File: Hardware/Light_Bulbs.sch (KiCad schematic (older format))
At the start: 29 parts, among them U1 PIC18F23K22

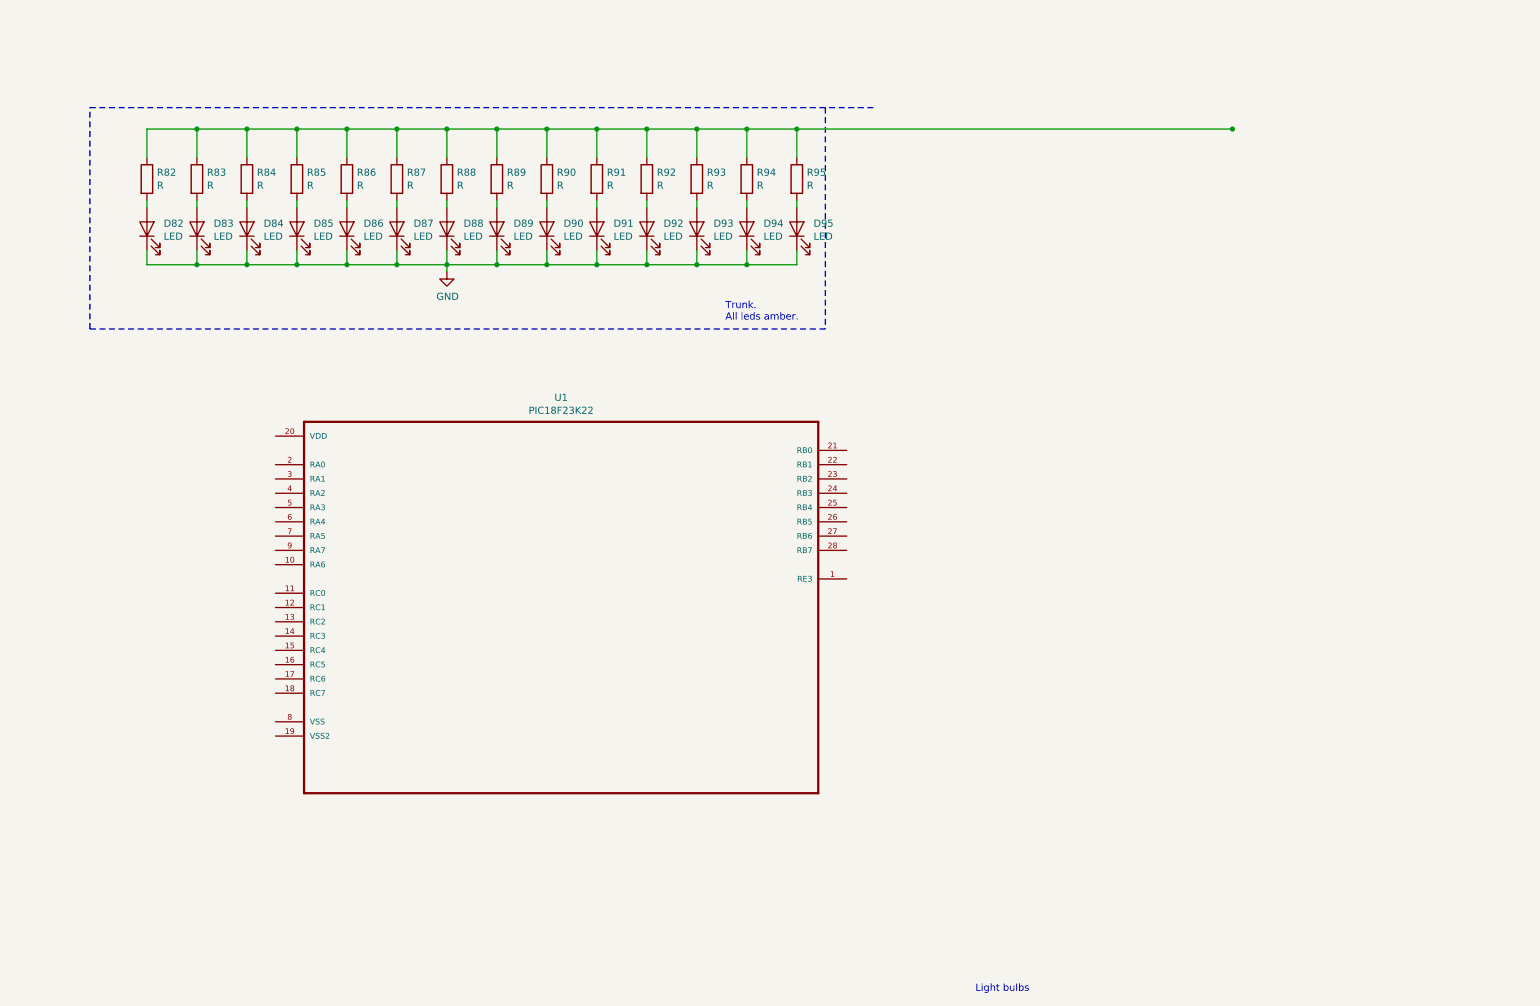
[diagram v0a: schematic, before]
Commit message: Added light bulbs schematic.
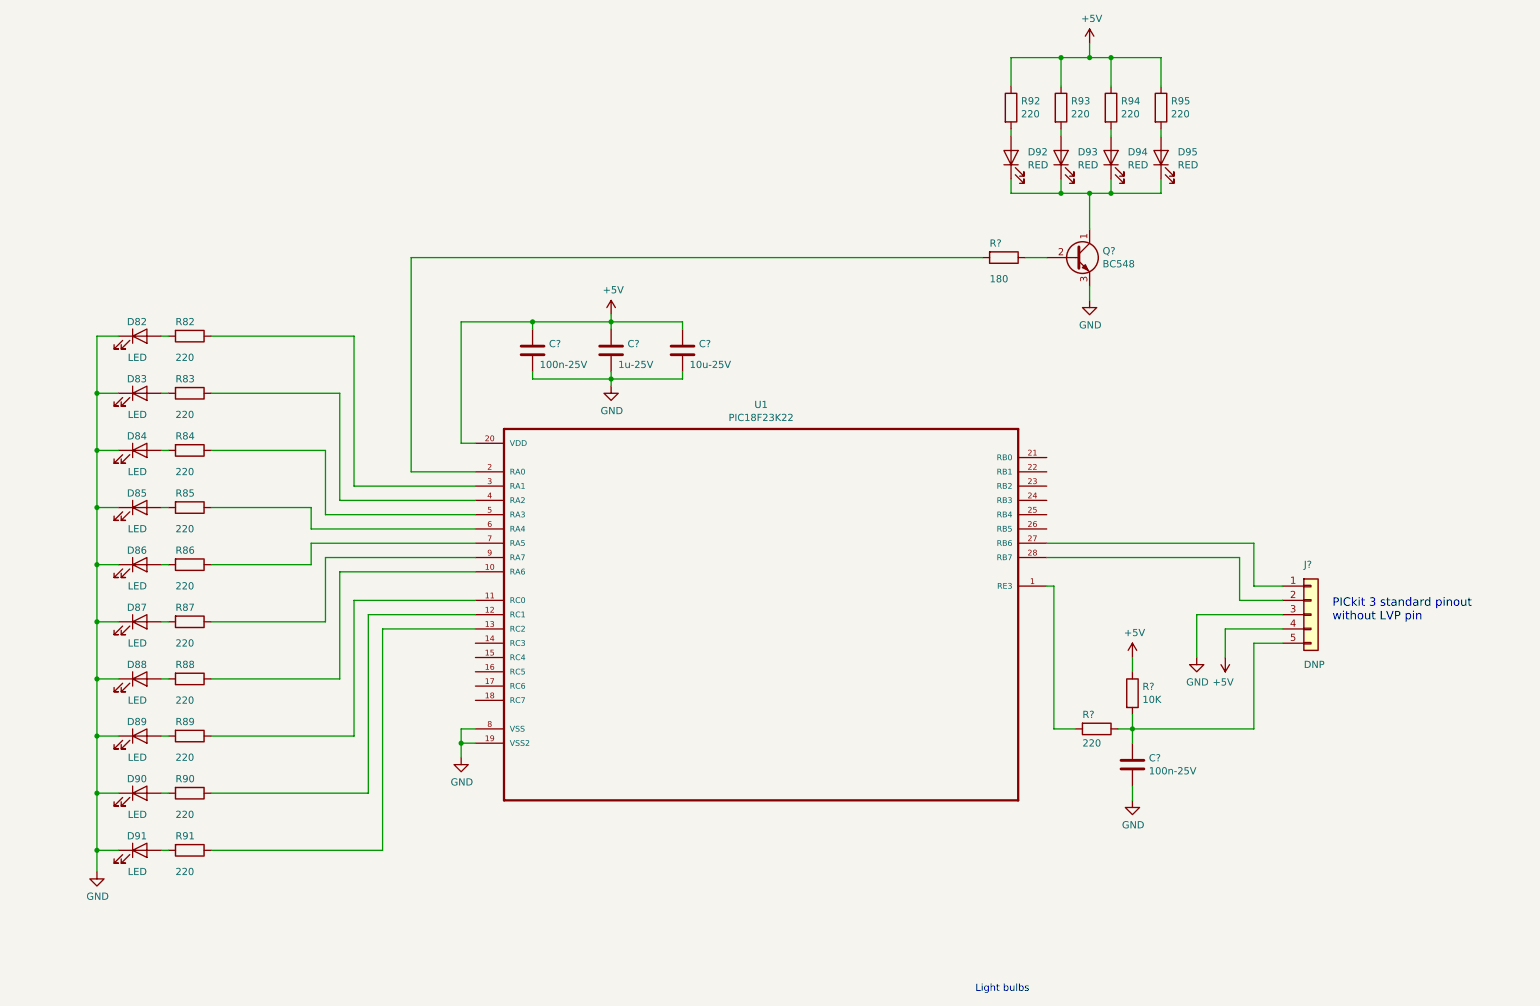
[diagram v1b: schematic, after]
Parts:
- added C?: 1u-25V, Capacitor_THT:C_Disc_D5.0mm_W2.5mm_P5.00mm, symbol Device:C
- added C?: 10u-25V, Capacitor_THT:C_Disc_D5.0mm_W2.5mm_P5.00mm, symbol Device:C
- added C? (x2): 100n-25V, Capacitor_THT:C_Disc_D5.0mm_W2.5mm_P5.00mm, symbol Device:C
- added J?: DNP, Connector_PinHeader_2.54mm:PinHeader_1x05_P2.54mm_Vertical, symbol Connector_Generic:Conn_01x05
- added Q?: BC548, Package_TO_SOT_THT:TO-92_Inline, symbol Transistor_BJT:BC548
- added R?: 180, Resistor_THT:R_Axial_DIN0207_L6.3mm_D2.5mm_P7.62mm_Horizontal, symbol Device:R
- added R?: 10K, Resistor_THT:R_Axial_DIN0207_L6.3mm_D2.5mm_P7.62mm_Horizontal, symbol Device:R
- added R?: 220, Resistor_THT:R_Axial_DIN0207_L6.3mm_D2.5mm_P7.62mm_Horizontal, symbol Device:R
- D92, D93, D94, D95: value LED -> RED
- R82, R83, R84, R85, R86, R87, R88, R89, R90, R91, R92, R93, R94, R95: value R -> 220
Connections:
- net GND: now also U1.19 (VSS2), U1.8 (VSS), C?.2, C?.2, C?.2, C?.2, J?.3 (Pin_3), Q?.3 (E); no longer D92.1 (K), D93.1 (K), D94.1 (K), D95.1 (K)
- net at U1.1 (RE3): now also R?.2
- net at U1.10 (RA6): now also R88.1
- net at U1.11 (RC0): now also R89.1
- net at U1.12 (RC1): now also R90.1
- net at U1.13 (RC2): now also R91.1
- net at U1.2 (RA0): now also R?.2
- net +5V: now reaches U1.20 (VDD)
- net +5V: now also R92.1, R93.1, R94.1, R95.1, C?.1, C?.1, C?.1, J?.4 (Pin_4), R?.1
- net at U1.27 (RB6): now also J?.1 (Pin_1)
- net at U1.28 (RB7): now also J?.2 (Pin_2)
- net at U1.3 (RA1): now also R82.1
- net at U1.4 (RA2): now also R83.1
- net at U1.5 (RA3): now also R84.1
- net at U1.6 (RA4): now also R85.1
- net at U1.7 (RA5): now also R86.1
- net at U1.9 (RA7): now also R87.1
- new net: C?.1, J?.5 (Pin_5), R?.1, R?.2
- new net: D92.1 (K), D93.1 (K), D94.1 (K), D95.1 (K), Q?.1 (C)
- new net: Q?.2 (B), R?.1
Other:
- note added: "PICkit 3 standard pinout\nwithout LVP pin"
- note removed: "Trunk.\nAll leds amber."
- moved on the sheet: D82, D83, D84, D85, D86, D87, D88, D89, D90, D91, D92, D93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

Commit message: Reorganized light bulbs connections to ease routing and placed microcontroller and related parts.
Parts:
- gave numbers to parts that had none: 9
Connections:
- net labels added: Bulb_0, Bulb_1, Bulb_2, Bulb_3, Bulb_4, Bulb_5, Bulb_6, Bulb_7, Bulb_8, Bulb_9, Star
- wire segments 127 -> 116
- no-connect marks 0 -> 11
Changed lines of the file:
@@
 Connection ~ 8350 1900
 $Comp
-L Transistor_BJT:BC548 Q?
+L Transistor_BJT:BC548 Q1
 U 1 1 5DE42A41
 P 8100 2350
-F 0 "Q?" H 8291 2396 50  0000 L CNN
+F 0 "Q1" H 8291 2396 50  0000 L CNN
 F 1 "BC548" H 8291 2305 50  0000 L CNN
 F 2 "Package_TO_SOT_THT:TO-92_Inline" H 8300 2275 50  0001 L CIN
@@
 P 8500 5400
 AR Path="/5DE1DFF6/5DFA145B" Ref="R?"  Part="1"
-AR Path="/5DE2A82E/5DFA145B" Ref="R?"  Part="1"
-F 0 "R?" H 8570 5446 50  0000 L CNN
+AR Path="/5DE2A82E/5DFA145B" Ref="R98"  Part="1"
+F 0 "R98" H 8570 5446 50  0000 L CNN
 F 1 "10K" H 8570 5355 50  0000 L CNN
 F 2 "Resistor_THT:R_Axial_DIN0207_L6.3mm_D2.5mm_P7.62mm_Horizontal" V 8430 5400 50  0001 C CNN
@@
 P 8250 5650
 AR Path="/5DE1DFF6/5DFA8AD3" Ref="R?"  Part="1"
-AR Path="/5DE2A82E/5DFA8AD3" Ref="R?"  Part="1"
-F 0 "R?" V 8150 5550 50  0000 L CNN
+AR Path="/5DE2A82E/5DFA8AD3" Ref="R97"  Part="1"
+F 0 "R97" V 8150 5550 50  0000 L CNN
 F 1 "220" V 8350 5550 50  0000 L CNN
 F 2 "Resistor_THT:R_Axial_DIN0207_L6.3mm_D2.5mm_P7.62mm_Horizontal" V 8180 5650 50  0001 C CNN
@@
 $EndComp
 $Comp
-L Device:C C?
+L Device:C C4
 U 1 1 5DFB7332
 P 8500 5900
-F 0 "C?" H 8615 5946 50  0000 L CNN
+F 0 "C4" H 8615 5946 50  0000 L CNN
 F 1 "100n-25V" H 8615 5855 50  0000 L CNN
 F 2 "Capacitor_THT:C_Disc_D5.0mm_W2.5mm_P5.00mm" H 8538 5750 50  0001 C CNN
@@
 	9550 4650 9350 4650
 $Comp
-L Connector_Generic:Conn_01x05 J?
+L Connector_Generic:Conn_01x05 J1
 U 1 1 5DDF0B46
 P 9750 4850
-F 0 "J?" H 9700 5200 50  0000 L CNN
+F 0 "J1" H 9700 5200 50  0000 L CNN
 F 1 "DNP" H 9700 4500 50  0000 L CNN
 F 2 "Connector_PinHeader_2.54mm:PinHeader_1x05_P2.54mm_Vertical" H 9750 4850 50  0001 C CNN
@@
 $EndComp
 $Comp
-L power:GND #PWR?
+L power:GND #PWR0106
 U 1 1 5DDF5E99
 P 3800 5850
-F 0 "#PWR?" H 3800 5600 50  0001 C CNN
+F 0 "#PWR0106" H 3800 5600 50  0001 C CNN
 F 1 "GND" H 3805 5677 50  0000 C CNN
 F 2 "" H 3800 5850 50  0001 C CNN
@@
 	3800 3650 3900 3650
 $Comp
-L Device:C C?
+L Device:C C1
 U 1 1 5DE05CC3
 P 4300 3000
-F 0 "C?" H 4415 3046 50  0000 L CNN
+F 0 "C1" H 4415 3046 50  0000 L CNN
 F 1 "100n-25V" H 4350 2900 50  0000 L CNN
 F 2 "Capacitor_THT:C_Disc_D5.0mm_W2.5mm_P5.00mm" H 4338 2850 50  0001 C CNN
@@
 $EndComp
 $Comp
-L Device:C C?
+L Device:C C2
 U 1 1 5DDF165E
 P 4850 3000
-F 0 "C?" H 4965 3046 50  0000 L CNN
+F 0 "C2" H 4965 3046 50  0000 L CNN
 F 1 "1u-25V" H 4900 2900 50  0000 L CNN
 F 2 "Capacitor_THT:C_Disc_D5.0mm_W2.5mm_P5.00mm" H 4888 2850 50  0001 C CNN
@@
 $EndComp
 $Comp
-L Device:C C?
+L Device:C C3
 U 1 1 5DDF2D76
 P 5350 3000
-F 0 "C?" H 5465 3046 50  0000 L CNN
+F 0 "C3" H 5465 3046 50  0000 L CNN
 F 1 "10u-25V" H 5400 2900 50  0000 L CNN
 F 2 "Capacitor_THT:C_Disc_D5.0mm_W2.5mm_P5.00mm" H 5388 2850 50  0001 C CNN
@@
 $EndComp
 $Comp
-L power:GND #PWR?
+L power:GND #PWR0109
 U 1 1 5DF0D1D6
 P 4850 3250
-F 0 "#PWR?" H 4850 3000 50  0001 C CNN
+F 0 "#PWR0109" H 4850 3000 50  0001 C CNN
 F 1 "GND" H 4855 3077 50  0000 C CNN
 F 2 "" H 4850 3250 50  0001 C CNN
@@
 	5350 3200 5350 3150
 $Comp
-L power:+5V #PWR?
+L power:+5V #PWR0114
 U 1 1 5DF13942
 P 4850 2750
-F 0 "#PWR?" H 4850 2600 50  0001 C CNN
+F 0 "#PWR0114" H 4850 2600 50  0001 C CNN
 F 1 "+5V" H 4865 2923 50  0000 C CNN
 F 2 "" H 4850 2750 50  0001 C CNN
@@
 	3800 2800 3800 3650
 Connection ~ 4300 2800
-Wire Wire Line
-	3900 3950 3050 3950
-Wire Wire Line
-	3050 3950 3050 2900
-Wire Wire Line
-	3050 2900 2050 2900
-Wire Wire Line
-	2950 4050 2950 3300
-Wire Wire Line
-	2950 3300 2050 3300
-Wire Wire Line
-	2950 4050 3900 4050
-Wire Wire Line
-	2850 4150 2850 3700
-Wire Wire Line
-	2850 3700 2050 3700
-Wire Wire Line
-	2850 4150 3900 4150
-Wire Wire Line
-	2750 4250 2750 4100
-Wire Wire Line
-	2750 4100 2050 4100
-Wire Wire Line
-	2750 4250 3900 4250
-Wire Wire Line
-	2050 4500 2750 4500
-Wire Wire Line
-	2750 4500 2750 4350
-Wire Wire Line
-	2750 4350 3900 4350
-Wire Wire Line
-	3900 4450 2850 4450
-Wire Wire Line
-	2850 4450 2850 4900
-Wire Wire Line
-	2850 4900 2050 4900
-Wire Wire Line
-	2050 5300 2950 5300
-Wire Wire Line
-	2950 5300 2950 4550
-Wire Wire Line
-	2950 4550 3900 4550
-Wire Wire Line
-	2050 5700 3050 5700
-Wire Wire Line
-	3050 5700 3050 4750
-Wire Wire Line
-	3050 4750 3900 4750
-Wire Wire Line
-	3900 4850 3150 4850
-Wire Wire Line
-	3150 4850 3150 6100
-Wire Wire Line
-	3150 6100 2050 6100
-Wire Wire Line
-	2050 6500 3250 6500
-Wire Wire Line
-	3250 6500 3250 4950
-Wire Wire Line
-	3250 4950 3900 4950
 $Comp
 L Device:R R?
@@
 P 7600 2350
 AR Path="/5DE1DFF6/5DE4BB6C" Ref="R?"  Part="1"
-AR Path="/5DE2A82E/5DE4BB6C" Ref="R?"  Part="1"
-F 0 "R?" V 7500 2250 50  0000 L CNN
+AR Path="/5DE2A82E/5DE4BB6C" Ref="R96"  Part="1"
+F 0 "R96" V 7500 2250 50  0000 L CNN
 F 1 "180" V 7750 2250 50  0000 L CNN
 F 2 "Resistor_THT:R_Axial_DIN0207_L6.3mm_D2.5mm_P7.62mm_Horizontal" V 7530 2350 50  0001 C CNN
@@
 Wire Wire Line
 	7750 2350 7900 2350
-Wire Wire Line
-	7450 2350 3450 2350
-Wire Wire Line
-	3450 2350 3450 3850
-Wire Wire Line
-	3450 3850 3900 3850
-$Comp
-L power:GND #PWR?
+$Comp
+L power:GND #PWR0115
 U 1 1 5DE5620F
 P 1250 6650
-F 0 "#PWR?" H 1250 6400 50  0001 C CNN
+F 0 "#PWR0115" H 1250 6400 50  0001 C CNN
 F 1 "GND" H 1255 6477 50  0000 C CNN
 F 2 "" H 1250 6650 50  0001 C CNN
@@
 	1250 2900 1400 2900
 Connection ~ 1250 3300
+Text Label 3600 5050 0    50   ~ 0
+Star
+Wire Wire Line
+	7450 2350 7200 2350
+Text Label 7200 2350 0    50   ~ 0
+Star
+Wire Wire Line
+	3900 4950 3600 4950
+Wire Wire Line
+	3600 5050 3900 5050
+Text Label 3600 4950 0    50   ~ 0
+Bulb_0
+Wire Wire Line
+	2050 2900 2300 2900
+Text Label 2050 2900 0    50   ~ 0
+Bulb_0
+Wire Wire Line
+	2050 3300 2300 3300
+Wire Wire Line
+	2050 3700 2300 3700
+Wire Wire Line
+	2050 4100 2300 4100
+Wire Wire Line
+	2050 4500 2300 4500
+Wire Wire Line
+	2050 4900 2300 4900
+Wire Wire Line
+	2050 5300 2300 5300
+Wire Wire Line
+	2050 5700 2300 5700
+Wire Wire Line
+	2050 6100 2300 6100
+Wire Wire Line
+	2050 6500 2300 6500
+Text Label 2050 3700 0    50   ~ 0
+Bulb_1
+Wire Wire Line
+	3900 4850 3600 4850
+Text Label 3600 4850 0    50   ~ 0
+Bulb_1
+Text Label 2050 4500 0    50   ~ 0
+Bulb_2
+Wire Wire Line
+	3900 4750 3600 4750
+Text Label 3600 4750 0    50   ~ 0
+Bulb_2
+Text Label 2050 5300 0    50   ~ 0
+Bulb_3
+Wire Wire Line
+	3900 4550 3600 4550
+Text Label 3600 4550 0    50   ~ 0
+Bulb_3
+Text Label 2050 6100 0    50   ~ 0
+Bulb_4
+Wire Wire Line
+	3900 4450 3600 4450
+Text Label 3600 4450 0    50   ~ 0
+Bulb_4
+Text Label 2050 3300 0    50   ~ 0
+Bulb_9
+Wire Wire Line
+	3900 5150 3600 5150
+Text Label 3600 5150 0    50   ~ 0
+Bulb_9
+Text Label 2050 4100 0    50   ~ 0
+Bulb_8
+Wire Wire Line
+	3900 5250 3600 5250
+Text Label 3600 5250 0    50   ~ 0
+Bulb_8
+Text Label 2050 4900 0    50   ~ 0
+Bulb_7
+Wire Wire Line
+	3900 5350 3600 5350
+Text Label 3600 5350 0    50   ~ 0
+Bulb_7
+Text Label 2050 5700 0    50   ~ 0
+Bulb_6
+Text Label 7950 4150 0    50   ~ 0
+Bulb_6
+Wire Wire Line
+	7900 4150 8200 4150
+Text Label 2050 6500 0    50   ~ 0
+Bulb_5
+Wire Wire Line
+	7900 4250 8200 4250
+Text Label 7950 4250 0    50   ~ 0
+Bulb_5
+NoConn ~ 7900 3750
+NoConn ~ 7900 3850
+NoConn ~ 7900 3950
+NoConn ~ 7900 4050
+NoConn ~ 3900 3850
+NoConn ~ 3900 3950
+NoConn ~ 3900 4050
+NoConn ~ 3900 4150
+NoConn ~ 3900 4250
+NoConn ~ 3900 4350
+NoConn ~ 3900 5450
 $EndSCHEMATC

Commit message: Added micro USB B connector for power supply.
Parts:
- added J2: USB_B_Micro, Connector_USB:USB_Micro-B_Molex-105017-0001, symbol Connector:USB_B_Micro
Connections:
- wire segments 116 -> 123
- no-connect marks 11 -> 14
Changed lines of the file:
@@
 NoConn ~ 3900 4350
 NoConn ~ 3900 5450
+$Comp
+L Connector:USB_B_Micro J2
+U 1 1 60874A52
+P 3000 1450
+F 0 "J2" H 3057 1917 50  0000 C CNN
+F 1 "USB_B_Micro" H 3057 1826 50  0000 C CNN
+F 2 "Connector_USB:USB_Micro-B_Molex-105017-0001" H 3150 1400 50  0001 C CNN
+F 3 "~" H 3150 1400 50  0001 C CNN
+	1    3000 1450
+	1    0    0    -1
+$EndComp
+$Comp
+L power:+5V #PWR0118
+U 1 1 60877195
+P 3450 1200
+F 0 "#PWR0118" H 3450 1050 50  0001 C CNN
+F 1 "+5V" H 3465 1373 50  0000 C CNN
+F 2 "" H 3450 1200 50  0001 C CNN
+F 3 "" H 3450 1200 50  0001 C CNN
+	1    3450 1200
+	1    0    0    -1
+$EndComp
+Wire Wire Line
+	3300 1250 3450 1250
+Wire Wire Line
+	3450 1250 3450 1200
+Wire Wire Line
+	2900 1850 2900 1950
+Wire Wire Line
+	2900 1950 2950 1950
+Wire Wire Line
+	3000 1950 3000 1850
+$Comp
+L power:GND #PWR0119
+U 1 1 6088078F
+P 2950 2000
+F 0 "#PWR0119" H 2950 1750 50  0001 C CNN
+F 1 "GND" H 2955 1827 50  0000 C CNN
+F 2 "" H 2950 2000 50  0001 C CNN
+F 3 "" H 2950 2000 50  0001 C CNN
+	1    2950 2000
+	1    0    0    -1
+$EndComp
+Wire Wire Line
+	2950 2000 2950 1950
+Connection ~ 2950 1950
+Wire Wire Line
+	2950 1950 3000 1950
+NoConn ~ 3300 1450
+NoConn ~ 3300 1550
+NoConn ~ 3300 1650
 $EndSCHEMATC

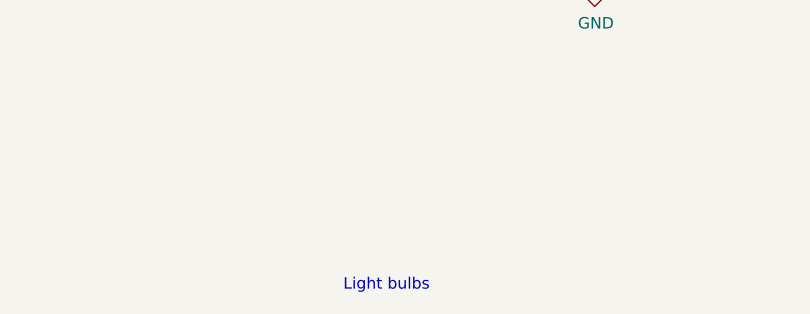
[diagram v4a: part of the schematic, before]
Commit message: Used standard schematic title blocks titles.
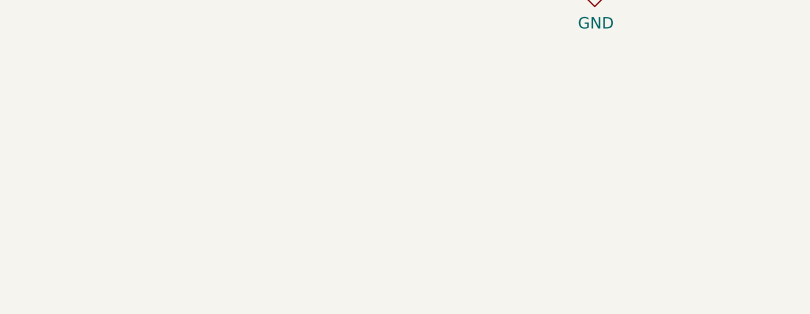
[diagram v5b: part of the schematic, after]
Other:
- note removed: "Light bulbs"
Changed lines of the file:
@@
 EESchema Schematic File Version 4
-LIBS:Chrismas_Tree-cache
 EELAYER 30 0
 EELAYER END
@@
 encoding utf-8
 Sheet 3 3
-Title ""
+Title "Light bulbs"
 Date ""
 Rev ""
-Comp ""
+Comp "Adrien RICCIARDI"
 Comment1 ""
 Comment2 ""
@@
 Comment4 ""
 $EndDescr
-Text Notes 7400 7500 0    50   ~ 0
-Light bulbs
 Wire Wire Line
 	1750 2900 1700 2900

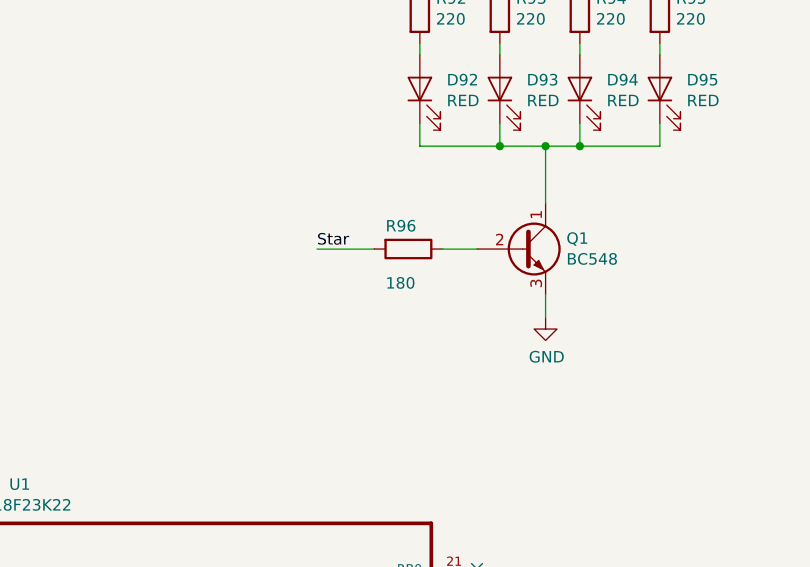
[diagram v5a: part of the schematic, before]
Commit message: Increased transitor base resistor value.
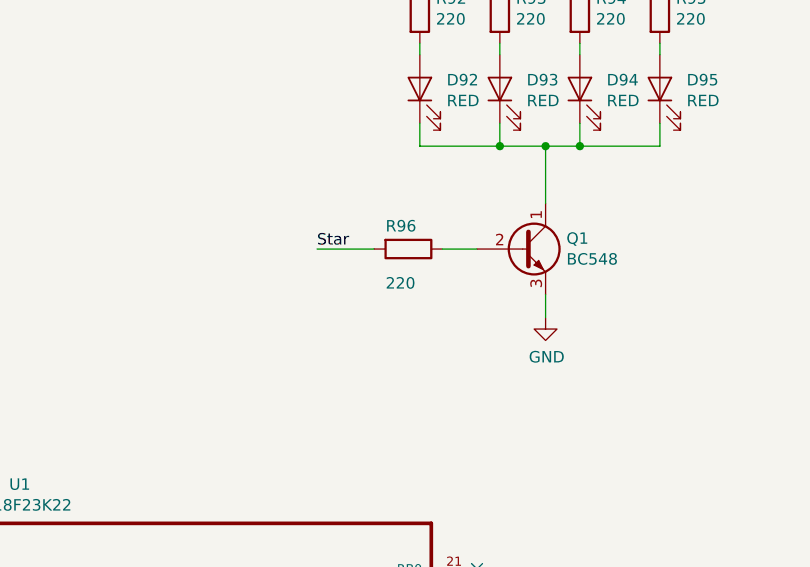
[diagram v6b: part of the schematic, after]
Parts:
- R96: value 180 -> 220
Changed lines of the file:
@@
 EESchema Schematic File Version 4
+LIBS:Chrismas_Tree-cache
 EELAYER 30 0
 EELAYER END
@@
 AR Path="/5DE2A82E/5DE4BB6C" Ref="R96"  Part="1"
 F 0 "R96" V 7500 2250 50  0000 L CNN
-F 1 "180" V 7750 2250 50  0000 L CNN
+F 1 "220" V 7750 2250 50  0000 L CNN
 F 2 "Resistor_THT:R_Axial_DIN0207_L6.3mm_D2.5mm_P7.62mm_Horizontal" V 7530 2350 50  0001 C CNN
 F 3 "~" H 7600 2350 50  0001 C CNN
